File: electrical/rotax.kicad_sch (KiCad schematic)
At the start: 15 parts

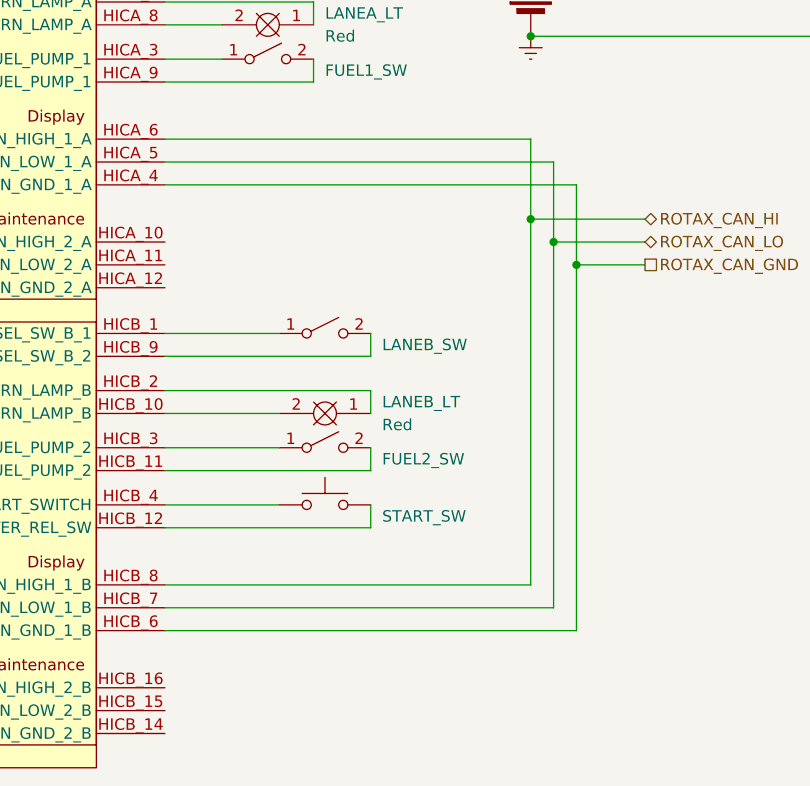
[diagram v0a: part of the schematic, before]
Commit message: Added Transponder and Navigator
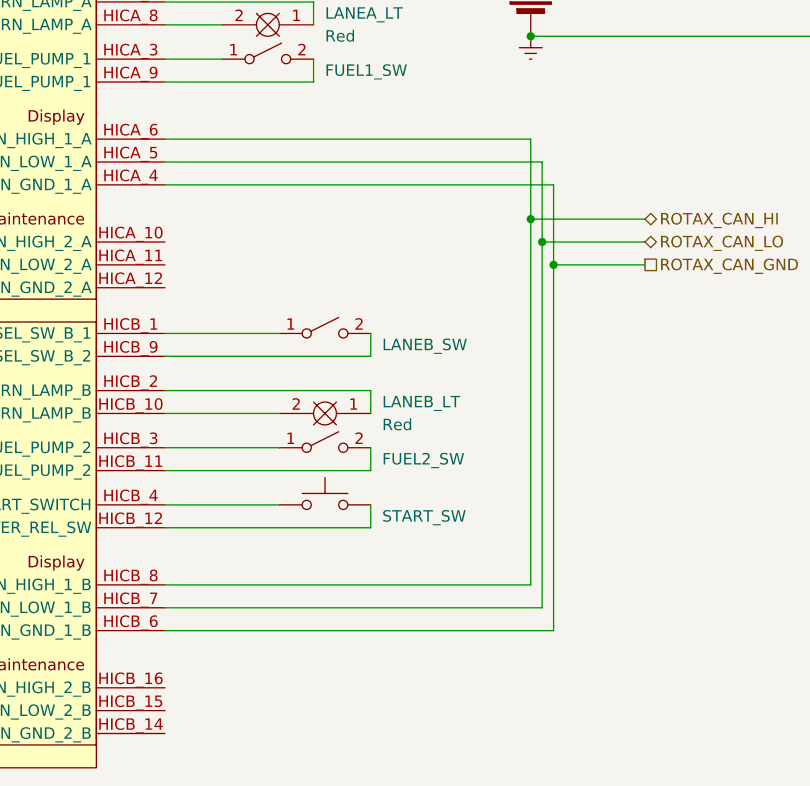
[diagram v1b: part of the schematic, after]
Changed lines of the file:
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@@
     (company "N915SN Angry Bird")
   )
-  (junction (at 130.81 113.03) (diameter 0) (color 0 0 0 0)
-  )
   (junction (at 228.6 74.93) (diameter 0) (color 0 0 0 0)
   )
@@
   (junction (at 181.61 67.31) (diameter 0) (color 0 0 0 0)
   )
-  (junction (at 133.35 115.57) (diameter 0) (color 0 0 0 0)
+  (junction (at 130.81 115.57) (diameter 0) (color 0 0 0 0)
+  )
+  (junction (at 129.54 113.03) (diameter 0) (color 0 0 0 0)
   )
   (junction (at 181.61 90.17) (diameter 0) (color 0 0 0 0)
@@
   (junction (at 201.93 57.15) (diameter 0) (color 0 0 0 0)
   )
-  (wire (pts (xy 130.81 113.03) (xy 140.97 113.03))
-    (stroke (width 0) (type default))
-  )
-  (wire (pts (xy 133.35 106.68) (xy 133.35 115.57))
+  (wire (pts (xy 130.81 106.68) (xy 130.81 115.57))
     (stroke (width 0) (type default))
   )
@@
     (stroke (width 0) (type default))
   )
+  (wire (pts (xy 129.54 113.03) (xy 140.97 113.03))
+    (stroke (width 0) (type default))
+  )
   (wire (pts (xy 87.63 52.07) (xy 238.76 52.07))
     (stroke (width 0) (type default))
@@
     (stroke (width 0) (type default))
   )
-  (wire (pts (xy 130.81 113.03) (xy 130.81 153.67))
-    (stroke (width 0) (type default))
-  )
-  (wire (pts (xy 140.97 115.57) (xy 133.35 115.57))
+  (wire (pts (xy 129.54 113.03) (xy 129.54 153.67))
+    (stroke (width 0) (type default))
+  )
+  (wire (pts (xy 130.81 115.57) (xy 140.97 115.57))
     (stroke (width 0) (type default))
   )
@@
     (stroke (width 0) (type default))
   )
-  (wire (pts (xy 87.63 106.68) (xy 133.35 106.68))
+  (wire (pts (xy 87.63 106.68) (xy 130.81 106.68))
     (stroke (width 0) (type default))
   )
@@
     (stroke (width 0) (type default))
   )
-  (wire (pts (xy 130.81 104.14) (xy 130.81 113.03))
+  (wire (pts (xy 129.54 104.14) (xy 129.54 113.03))
     (stroke (width 0) (type default))
   )
@@
     (stroke (width 0) (type default))
   )
-  (wire (pts (xy 130.81 153.67) (xy 87.63 153.67))
-    (stroke (width 0) (type default))
-  )
-  (wire (pts (xy 133.35 156.21) (xy 87.63 156.21))
+  (wire (pts (xy 129.54 153.67) (xy 87.63 153.67))
+    (stroke (width 0) (type default))
+  )
+  (wire (pts (xy 130.81 156.21) (xy 87.63 156.21))
     (stroke (width 0) (type default))
   )
@@
     (stroke (width 0) (type default))
   )
-  (wire (pts (xy 133.35 115.57) (xy 133.35 156.21))
+  (wire (pts (xy 130.81 115.57) (xy 130.81 156.21))
     (stroke (width 0) (type default))
   )
@@
     (stroke (width 0) (type default))
   )
-  (wire (pts (xy 130.81 104.14) (xy 87.63 104.14))
-    (stroke (width 0) (type default))
-  )
+  (wire (pts (xy 129.54 104.14) (xy 87.63 104.14))
+    (stroke (width 0) (type default))
+  )

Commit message: Added EIS
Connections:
- net ROTAX_CAN_GND: no longer names the net of 915iS.HICA_4 (CAN_GND_1_A), 915iS.HICB_6 (CAN_GND_1_B)
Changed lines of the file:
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@@
   (junction (at 181.61 67.31) (diameter 0) (color 0 0 0 0)
   )
-  (junction (at 130.81 115.57) (diameter 0) (color 0 0 0 0)
-  )
   (junction (at 129.54 113.03) (diameter 0) (color 0 0 0 0)
   )
@@
   (junction (at 201.93 57.15) (diameter 0) (color 0 0 0 0)
   )
-  (wire (pts (xy 130.81 106.68) (xy 130.81 115.57))
-    (stroke (width 0) (type default))
-  )
   (wire (pts (xy 92.71 73.66) (xy 92.71 57.15))
     (stroke (width 0) (type default))
@@
     (stroke (width 0) (type default))
   )
-  (wire (pts (xy 130.81 115.57) (xy 140.97 115.57))
-    (stroke (width 0) (type default))
-  )
   (wire (pts (xy 87.63 92.71) (xy 93.98 92.71))
     (stroke (width 0) (type default))
@@
     (stroke (width 0) (type default))
   )
-  (wire (pts (xy 130.81 115.57) (xy 130.81 156.21))
+  (wire (pts (xy 130.81 106.68) (xy 130.81 156.21))
     (stroke (width 0) (type default))
   )
@@
     (effects (font (size 1.27 1.27)) (justify left))
   )
-  (hierarchical_label "ROTAX_CAN_GND" (shape passive) (at 140.97 115.57 0) (fields_autoplaced)
-    (effects (font (size 1.27 1.27)) (justify left))
-  )

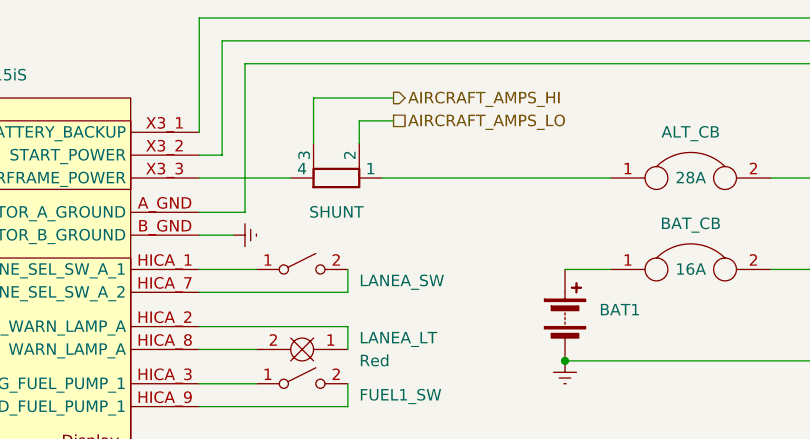
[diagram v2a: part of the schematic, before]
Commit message: Removed Amps as Rotax sends that over Can to GEA24
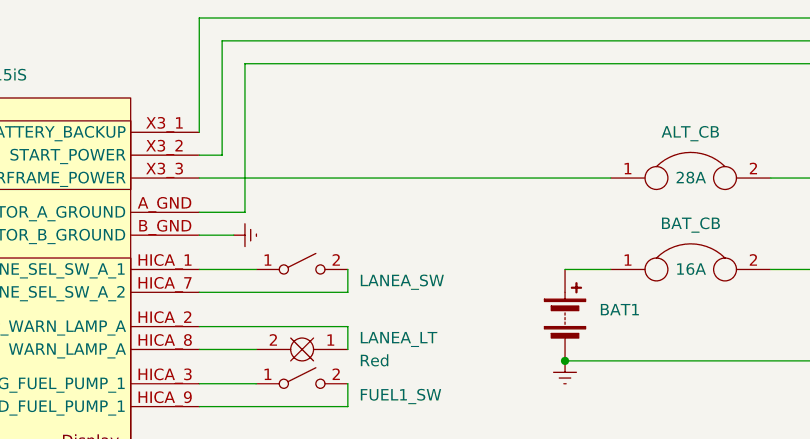
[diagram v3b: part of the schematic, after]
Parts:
- removed SHUNT: R_Shunt, symbol Device:R_Shunt
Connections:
- net at ALT_CB.1: now also 915iS.X3_3 (AIRFRAME_POWER)
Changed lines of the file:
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@@
-    (stroke (width 0) (type default))
-  )
-  (wire (pts (xy 109.22 63.5) (xy 105.41 63.5))
     (stroke (width 0) (type default))
   )
@@
     (stroke (width 0) (type default))
   )
-  (wire (pts (xy 109.22 60.96) (xy 100.33 60.96))
-    (stroke (width 0) (type default))
-  )
   (wire (pts (xy 128.27 101.6) (xy 87.63 101.6))
     (stroke (width 0) (type default))
@@
     (stroke (width 0) (type default))
   )
-  (wire (pts (xy 100.33 60.96) (xy 100.33 66.04))
-    (stroke (width 0) (type default))
-  )
   (wire (pts (xy 110.49 135.89) (xy 110.49 138.43))
     (stroke (width 0) (type default))
@@
     (stroke (width 0) (type default))
   )
-  (wire (pts (xy 87.63 69.85) (xy 97.79 69.85))
-    (stroke (width 0) (type default))
-  )
   (wire (pts (xy 104.14 92.71) (xy 104.14 95.25))
     (stroke (width 0) (type default))
@@
     (stroke (width 0) (type default))
   )
-  (wire (pts (xy 107.95 69.85) (xy 133.35 69.85))
-    (stroke (width 0) (type default))
-  )
   (wire (pts (xy 201.93 67.31) (xy 209.55 67.31))
     (stroke (width 0) (type default))
@@
     (stroke (width 0) (type default))
   )
-  (wire (pts (xy 105.41 63.5) (xy 105.41 66.04))
+  (wire (pts (xy 87.63 69.85) (xy 133.35 69.85))
     (stroke (width 0) (type default))
   )
@@
     (stroke (width 0) (type default))
   )
-  (hierarchical_label "AIRCRAFT_AMPS_HI" (shape output) (at 109.22 60.96 0) (fields_autoplaced)
-    (effects (font (size 1.27 1.27)) (justify left))
-  )
   (hierarchical_label "ROTAX_CAN_LO" (shape bidirectional) (at 140.97 113.03 0) (fields_autoplaced)
     (effects (font (size 1.27 1.27)) (justify left))
@@
   )
   (hierarchical_label "ROTAX_CAN_HI" (shape bidirectional) (at 140.97 110.49 0) (fields_autoplaced)
-    (effects (font (size 1.27 1.27)) (justify left))
-  )
-  (hierarchical_label "AIRCRAFT_AMPS_LO" (shape passive) (at 109.22 63.5 0) (fields_autoplaced)
     (effects (font (size 1.27 1.27)) (justify left))
   )
@@
         )
       )
-    )
-  )
-  (symbol (lib_id "Device:R_Shunt") (at 102.87 69.85 270) (mirror x) (unit 1)
-    (in_bom yes) (on_board yes) (dnp no)
-    (property "Reference" "SHUNT" (at 102.87 73.66 90)
-      (effects (font (size 1.27 1.27)))
-    )
-    (property "Value" "R_Shunt" (at 102.87 73.66 90)
-      (effects (font (size 1.27 1.27)) hide)
-    )
-    (property "Footprint" "" (at 102.87 71.628 90)
-      (effects (font (size 1.27 1.27)) hide)
-    )
-    (property "Datasheet" "~" (at 102.87 69.85 0)
-      (effects (font (size 1.27 1.27)) hide)
-    )
-    (pin "3")
-    (pin "1")
-    (pin "4")
-    (pin "2")
-    (instances
-      (project "N915SN"
-        (path "/c752466a-539c-4874-9d29-5b371a78af77/60dab9d2-c9f8-4000-bf71-d15a16d07db7"
-          (reference "SHUNT") (unit 1)
-        )
-      )
-      (project "electrical"
-        (path "/e8ec215a-dbe2-4eba-a577-e50a0a128049/2dfb13c9-19ab-4b61-8910-6455da71626b"
-          (reference "SHUNT") (unit 1)
-        )
-      )

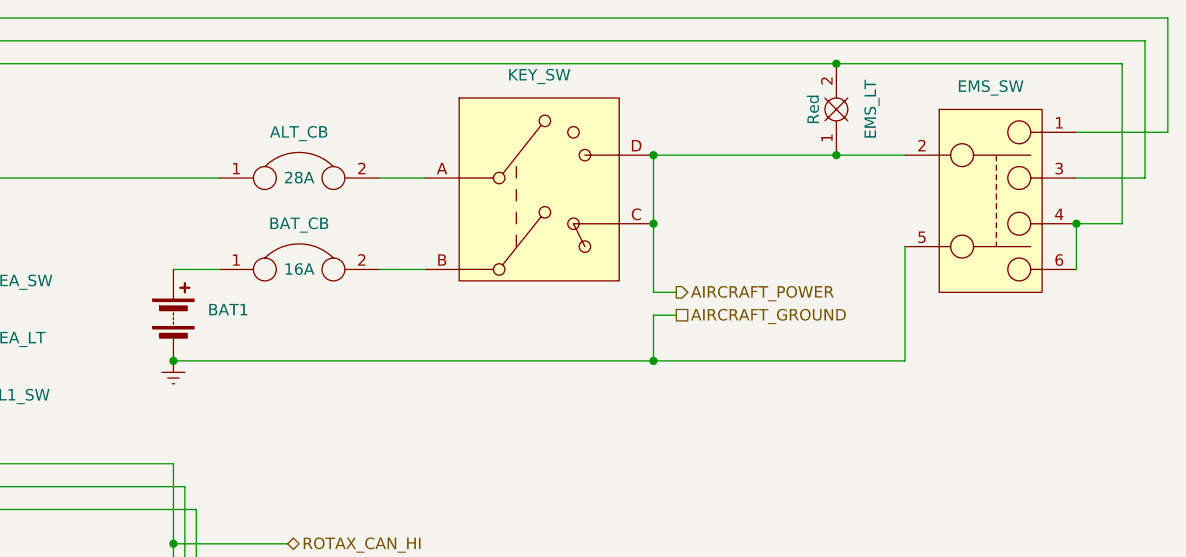
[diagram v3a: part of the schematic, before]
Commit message: Changed EMS and Start Power to work like Kitfox
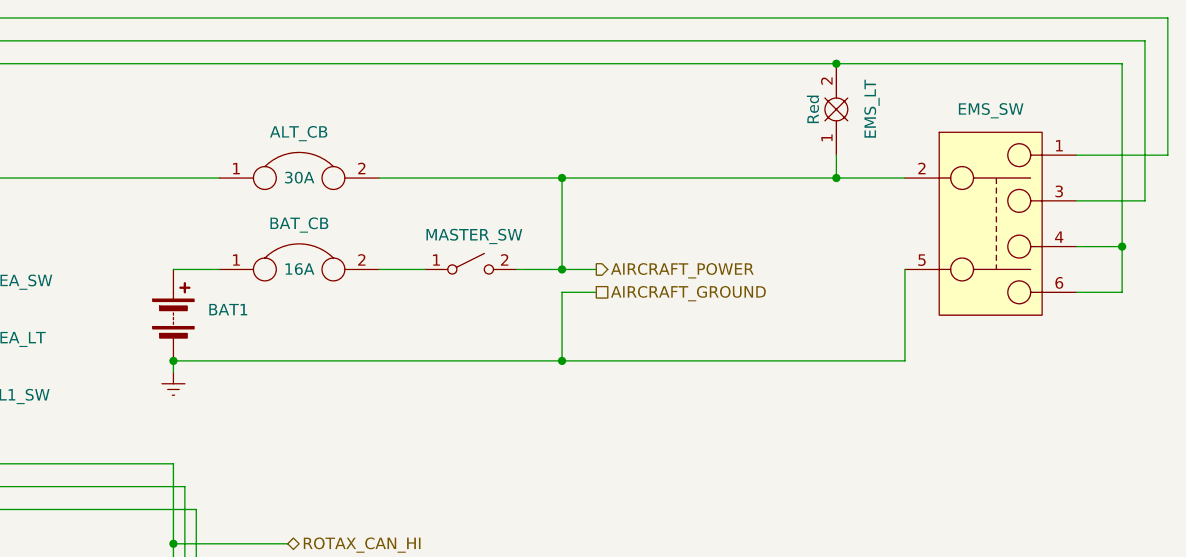
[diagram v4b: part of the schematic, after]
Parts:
- removed KEY_SW: Honeywell 84826, symbol flyerx:Honeywell 84826
- added MASTER_SW: ~, symbol Switch:SW_SPST
- ALT_CB: value 28A -> 30A
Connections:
- net AIRCRAFT_POWER: now also ALT_CB.2, MASTER_SW.2 (B)
- net at BAT_CB.2: now also MASTER_SW.1 (A)
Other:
- moved on the sheet: EMS_SW

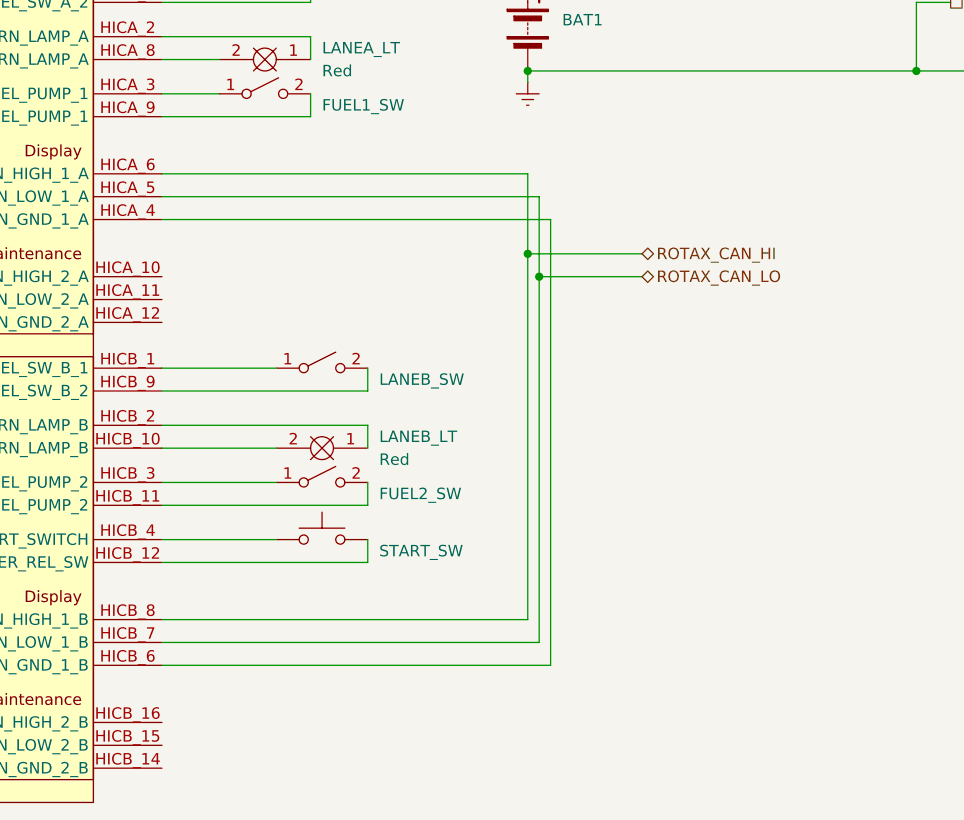
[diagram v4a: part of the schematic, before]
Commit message: Changed Rotax Canbus to be 2 connections
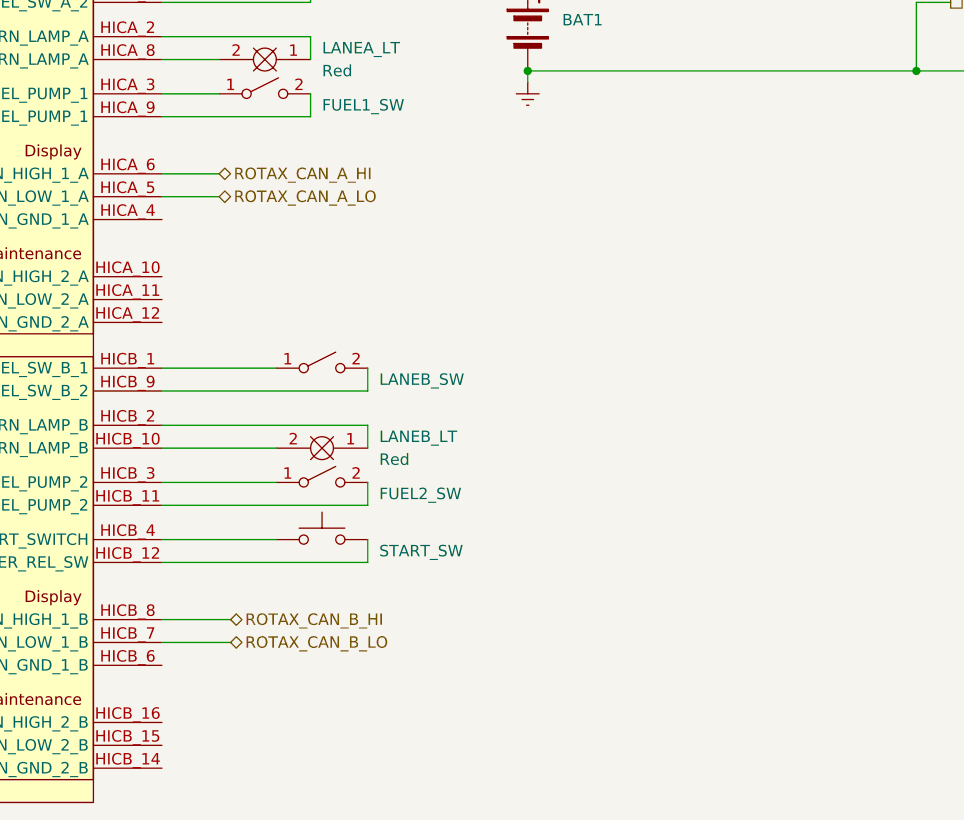
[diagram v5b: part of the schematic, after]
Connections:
- net at 915iS.HICA_4 (CAN_GND_1_A): no longer 915iS.HICB_6 (CAN_GND_1_B)
- net ROTAX_CAN_HI renamed ROTAX_CAN_A_HI
- net ROTAX_CAN_A_HI: no longer 915iS.HICB_8 (CAN_HIGH_1_B)
- net ROTAX_CAN_LO renamed ROTAX_CAN_A_LO
- net ROTAX_CAN_A_LO: no longer 915iS.HICB_7 (CAN_LOW_1_B)
- new net ROTAX_CAN_B_HI: 915iS.HICB_8 (CAN_HIGH_1_B)
- new net ROTAX_CAN_B_LO: 915iS.HICB_7 (CAN_LOW_1_B)
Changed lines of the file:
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@@
   (junction (at 128.27 90.17) (diameter 0) (color 0 0 0 0)
   )
-  (junction (at 128.27 110.49) (diameter 0) (color 0 0 0 0)
-  )
   (junction (at 171.45 90.17) (diameter 0) (color 0 0 0 0)
   )
   (junction (at 171.45 69.85) (diameter 0) (color 0 0 0 0)
   )
-  (junction (at 129.54 113.03) (diameter 0) (color 0 0 0 0)
-  )
   (junction (at 171.45 80.01) (diameter 0) (color 0 0 0 0)
   )
@@
     (stroke (width 0) (type default))
   )
-  (wire (pts (xy 129.54 113.03) (xy 140.97 113.03))
-    (stroke (width 0) (type default))
-  )
   (wire (pts (xy 87.63 52.07) (xy 238.76 52.07))
     (stroke (width 0) (type default))
@@
     (stroke (width 0) (type default))
   )
-  (wire (pts (xy 128.27 151.13) (xy 87.63 151.13))
-    (stroke (width 0) (type default))
-  )
   (wire (pts (xy 171.45 90.17) (xy 171.45 82.55))
     (stroke (width 0) (type default))
   )
-  (wire (pts (xy 128.27 110.49) (xy 128.27 151.13))
-    (stroke (width 0) (type default))
-  )
   (wire (pts (xy 201.93 57.15) (xy 233.68 57.15))
     (stroke (width 0) (type default))
@@
     (stroke (width 0) (type default))
   )
-  (wire (pts (xy 129.54 113.03) (xy 129.54 153.67))
-    (stroke (width 0) (type default))
-  )
   (wire (pts (xy 87.63 92.71) (xy 93.98 92.71))
     (stroke (width 0) (type default))
@@
     (stroke (width 0) (type default))
   )
-  (wire (pts (xy 128.27 101.6) (xy 87.63 101.6))
+  (wire (pts (xy 87.63 101.6) (xy 93.98 101.6))
     (stroke (width 0) (type default))
   )
@@
     (stroke (width 0) (type default))
   )
-  (wire (pts (xy 87.63 106.68) (xy 130.81 106.68))
-    (stroke (width 0) (type default))
-  )
   (wire (pts (xy 110.49 135.89) (xy 110.49 138.43))
     (stroke (width 0) (type default))
   )
+  (wire (pts (xy 87.63 153.67) (xy 95.25 153.67))
+    (stroke (width 0) (type default))
+  )
   (wire (pts (xy 104.14 92.71) (xy 104.14 95.25))
     (stroke (width 0) (type default))
   )
-  (wire (pts (xy 128.27 110.49) (xy 140.97 110.49))
-    (stroke (width 0) (type default))
-  )
-  (wire (pts (xy 128.27 101.6) (xy 128.27 110.49))
+  (wire (pts (xy 87.63 151.13) (xy 95.25 151.13))
     (stroke (width 0) (type default))
   )
@@
     (stroke (width 0) (type default))
   )
-  (wire (pts (xy 129.54 104.14) (xy 129.54 113.03))
-    (stroke (width 0) (type default))
-  )
   (wire (pts (xy 91.44 76.2) (xy 87.63 76.2))
     (stroke (width 0) (type default))
@@
     (stroke (width 0) (type default))
   )
-  (wire (pts (xy 129.54 153.67) (xy 87.63 153.67))
-    (stroke (width 0) (type default))
-  )
-  (wire (pts (xy 130.81 156.21) (xy 87.63 156.21))
-    (stroke (width 0) (type default))
-  )
   (wire (pts (xy 87.63 69.85) (xy 133.35 69.85))
     (stroke (width 0) (type default))
@@
     (stroke (width 0) (type default))
   )
-  (wire (pts (xy 130.81 106.68) (xy 130.81 156.21))
-    (stroke (width 0) (type default))
-  )
   (wire (pts (xy 228.6 82.55) (xy 233.68 82.55))
     (stroke (width 0) (type default))
@@
     (stroke (width 0) (type default))
   )
-  (wire (pts (xy 129.54 104.14) (xy 87.63 104.14))
+  (wire (pts (xy 87.63 104.14) (xy 93.98 104.14))
     (stroke (width 0) (type default))
   )
@@
     (stroke (width 0) (type default))
   )
-  (hierarchical_label "ROTAX_CAN_LO" (shape bidirectional) (at 140.97 113.03 0) (fields_autoplaced)
+  (hierarchical_label "ROTAX_CAN_B_LO" (shape bidirectional) (at 95.25 153.67 0) (fields_autoplaced)
+    (effects (font (size 1.27 1.27)) (justify left))
+  )
+  (hierarchical_label "ROTAX_CAN_A_LO" (shape bidirectional) (at 93.98 104.14 0) (fields_autoplaced)
+    (effects (font (size 1.27 1.27)) (justify left))
+  )
+  (hierarchical_label "ROTAX_CAN_B_HI" (shape bidirectional) (at 95.25 151.13 0) (fields_autoplaced)
     (effects (font (size 1.27 1.27)) (justify left))
   )
@@
     (effects (font (size 1.27 1.27)) (justify left))
   )
-  (hierarchical_label "ROTAX_CAN_HI" (shape bidirectional) (at 140.97 110.49 0) (fields_autoplaced)
-    (effects (font (size 1.27 1.27)) (justify left))
-  )
+  (hierarchical_label "ROTAX_CAN_A_HI" (shape bidirectional) (at 93.98 101.6 0) (fields_autoplaced)
+    (effects (font (size 1.27 1.27)) (justify left))
+  )
